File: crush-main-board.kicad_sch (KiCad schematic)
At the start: 32 parts, among them J1 4x4_Header, J10 3x3 Header, J11 3x3 Header, J12 3x2 Header, J13 3x4_Header, J14 3x4_Header, J15 2157601008, J16 Conn_01x02, J17 Conn_01x02, J2 4x4_Header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

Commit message: Fixed import issues from sch to pcb
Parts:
- J1: footprint Crush_Mainboard_Footprints:3x1_Header -> Crush_Mainboard_Footprints:4x4_Header
- U5, U6: renamed from INA232B1; value ~ -> INA232B
- U5: value ISO1640DBR -> ISO1640BDR; footprint Crush_Mainboard_Footprints:SOIC127P1030X265-16N -> Package_SO:SOIC-8_3.9x4.9mm_P1.27mm
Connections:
- net +3V3: now also U5.1 (VCC1); no longer U5.3 (VCC1)
- net +3V3_T: now also U5.8 (VCC2); no longer U5.14 (VCC2)
- net GND_T: now also U5.4 (GND1), U5.5 (GND2); no longer U5.7 (GND1), U5.9 (GND2)
- net SCL_3V3: now also U5.3 (SCL1); no longer U5.6 (SCL1)
- net SCL_T: now also U5.6 (SCL2); no longer U5.11 (SCL2)
- net SDA_3V3: now also U5.2 (SDA1); no longer U5.5 (SDA1)
- net SDA_T: now also U5.7 (SDA2); no longer U5.12 (SDA2)
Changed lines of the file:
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@@
       (effects (font (size 1.27 1.27)))
     )
-    (property "Footprint" "Crush_Mainboard_Footprints:3x1_Header" (at 255.8034 281.2796 0)
+    (property "Footprint" "Crush_Mainboard_Footprints:4x4_Header" (at 255.8034 281.2796 0)
       (effects (font (size 1.27 1.27)) (justify bottom) hide)
     )
@@
   )
   (symbol (lib_id "Crush_MainBoard_Symbols:INA232") (at 154.94 77.47 0) (unit 1)
-    (in_bom yes) (on_board yes) (dnp no) (fields_autoplaced)
-    (property "Reference" "INA232B1" (at 157.1341 66.04 0)
+    (in_bom yes) (on_board yes) (dnp no)
+    (property "Reference" "U5" (at 158.115 64.77 0)
       (effects (font (size 1.27 1.27)) (justify left))
     )
-    (property "Value" "~" (at 154.94 78.74 0)
+    (property "Value" "INA232B" (at 160.02 67.31 0)
       (effects (font (size 1.27 1.27)))
     )
@@
       (project "crush-main-board"
         (path "/74b566fe-9d71-4817-95ed-d472d647f8c8"
-          (reference "INA232B2") (unit 1)
+          (reference "U5") (unit 1)
         )
       )
@@
       (effects (font (size 1.27 1.27)))
     )
-    (property "Value" "ISO1640DBR" (at 205.74 114.3 0)
-      (effects (font (size 1.27 1.27)))
-    )
-    (property "Footprint" "Crush_Mainboard_Footprints:SOIC127P1030X265-16N" (at 205.74 134.62 0)
+    (property "Value" "ISO1640BDR" (at 205.74 114.3 0)
+      (effects (font (size 1.27 1.27)))
+    )
+    (property "Footprint" "Package_SO:SOIC-8_3.9x4.9mm_P1.27mm" (at 205.74 134.62 0)
       (effects (font (size 1.27 1.27)) hide)
     )
@@
       (effects (font (size 1.27 1.27)) hide)
     )
-    (pin "11")
-    (pin "12")
-    (pin "14")
+    (pin "1")
+    (pin "2")
+    (pin "8")
     (pin "3")
     (pin "5")
     (pin "6")
     (pin "7")
-    (pin "9")
+    (pin "4")
     (instances
       (project "battery_monitor"
@@
   )
   (symbol (lib_id "Connector_Generic:Conn_01x02") (at 234.95 210.82 180) (unit 1)
-    (in_bom yes) (on_board yes) (dnp no) (fields_autoplaced)
-    (property "Reference" "J16" (at 234.95 203.2 0)
+    (in_bom yes) (on_board yes) (dnp no)
+    (property "Reference" "J16" (at 231.14 209.55 0)
       (effects (font (size 1.27 1.27)))
     )
@@
   )
   (symbol (lib_id "Crush_MainBoard_Symbols:INA232") (at 154.94 128.27 0) (unit 1)
-    (in_bom yes) (on_board yes) (dnp no) (fields_autoplaced)
-    (property "Reference" "INA232B1" (at 157.1341 116.84 0)
+    (in_bom yes) (on_board yes) (dnp no)
+    (property "Reference" "U6" (at 157.48 115.57 0)
       (effects (font (size 1.27 1.27)) (justify left))
     )
-    (property "Value" "~" (at 154.94 129.54 0)
+    (property "Value" "INA232B" (at 160.02 118.11 0)
       (effects (font (size 1.27 1.27)))
     )
@@
       (project "crush-main-board"
         (path "/74b566fe-9d71-4817-95ed-d472d647f8c8"
-          (reference "INA232B1") (unit 1)
+          (reference "U6") (unit 1)
         )
       )
@@
   )
   (symbol (lib_id "Connector_Generic:Conn_01x02") (at 234.95 219.71 180) (unit 1)
-    (in_bom yes) (on_board yes) (dnp no) (fields_autoplaced)
-    (property "Reference" "J17" (at 234.95 212.09 0)
-      (effects (font (size 1.27 1.27)))
-    )
+    (in_bom yes) (on_board yes) (dnp no)
+    (property "Reference" "J17" (at 230.505 218.44 0)
+      (effects (font (size 1.27 1.27)))
+    )

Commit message: basic routing
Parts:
- added H1, H2, H3, H4: MountingHole_Pad, MountingHole:MountingHole_4.3mm_M4_Pad_Via, symbol Mechanical:MountingHole_Pad
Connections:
- net GND: now also H1.1, H2.1, H3.1, H4.1
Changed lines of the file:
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@@
     (rev "1")
   )
+  (junction (at 377.19 149.86) (diameter 0) (color 0 0 0 0)
+  )
+  (junction (at 377.19 154.94) (diameter 0) (color 0 0 0 0)
+  )
   (junction (at 97.155 252.73) (diameter 0) (color 0 0 0 0)
   )
@@
   (junction (at 321.31 253.365) (diameter 0) (color 0 0 0 0)
   )
+  (junction (at 377.19 144.78) (diameter 0) (color 0 0 0 0)
+  )
   (junction (at 321.31 206.375) (diameter 0) (color 0 0 0 0)
   )
@@
     (stroke (width 0) (type default))
   )
+  (wire (pts (xy 377.19 157.48) (xy 377.19 154.94))
+    (stroke (width 0) (type default))
+  )
   (wire (pts (xy 290.83 213.36) (xy 290.83 215.9))
     (stroke (width 0) (type default))
@@
     (stroke (width 0) (type default))
   )
+  (wire (pts (xy 377.19 154.94) (xy 379.73 154.94))
+    (stroke (width 0) (type default))
+  )
   (wire (pts (xy 239.2934 270.4846) (xy 241.8334 270.4846))
     (stroke (width 0) (type default))
@@
     (stroke (width 0) (type default))
   )
+  (wire (pts (xy 377.19 144.78) (xy 379.73 144.78))
+    (stroke (width 0) (type default))
+  )
   (wire (pts (xy 386.08 42.545) (xy 386.08 45.085))
     (stroke (width 0) (type default))
@@
     (stroke (width 0) (type default))
   )
+  (wire (pts (xy 377.19 149.86) (xy 377.19 144.78))
+    (stroke (width 0) (type default))
+  )
   (wire (pts (xy 239.2934 267.9446) (xy 239.2934 270.4846))
     (stroke (width 0) (type default))
@@
     (stroke (width 0) (type default))
   )
+  (wire (pts (xy 377.19 144.78) (xy 377.19 139.7))
+    (stroke (width 0) (type default))
+  )
   (wire (pts (xy 321.31 253.365) (xy 321.31 250.825))
     (stroke (width 0) (type default))
@@
     (stroke (width 0) (type default))
   )
+  (wire (pts (xy 377.19 149.86) (xy 379.73 149.86))
+    (stroke (width 0) (type default))
+  )
   (wire (pts (xy 97.155 255.27) (xy 94.615 255.27))
     (stroke (width 0) (type default))
@@
     (stroke (width 0) (type default))
   )
+  (wire (pts (xy 377.19 139.7) (xy 379.73 139.7))
+    (stroke (width 0) (type default))
+  )
   (wire (pts (xy 194.31 106.68) (xy 193.04 106.68))
     (stroke (width 0) (type default))
@@
     (stroke (width 0) (type default))
   )
+  (wire (pts (xy 377.19 154.94) (xy 377.19 149.86))
+    (stroke (width 0) (type default))
+  )
   (wire (pts (xy 162.56 255.27) (xy 162.56 257.81))
     (stroke (width 0) (type default))
@@
     (effects (font (size 2 2)) (justify left top))
   )
+  (text_box "Mounting Holes"
+    (at 373.38 133.35 0) (size 33.02 31.75)
+    (stroke (width 0) (type dash))
+    (fill (type none))
+    (effects (font (size 1.27 1.27)) (justify left top))
+  )
   (text_box "Analog&Digital_Headers"
     (at 12.827 209.169 0) (size 91.694 73.66)
@@
     )
   )
+  (symbol (lib_id "Mechanical:MountingHole_Pad") (at 382.27 139.7 270) (unit 1)
+    (in_bom yes) (on_board yes) (dnp no) (fields_autoplaced)
+    (property "Reference" "H1" (at 386.08 138.43 90)
+      (effects (font (size 1.27 1.27)) (justify left))
+    )
+    (property "Value" "MountingHole_Pad" (at 386.08 140.97 90)
+      (effects (font (size 1.27 1.27)) (justify left))
+    )
+    (property "Footprint" "MountingHole:MountingHole_4.3mm_M4_Pad_Via" (at 382.27 139.7 0)
+      (effects (font (size 1.27 1.27)) hide)
+    )
+    (property "Datasheet" "" (at 382.27 139.7 0)
+      (effects (font (size 1.27 1.27)) hide)
+    )
+    (pin "1")
+    (instances
+      (project "crush-main-board"
+        (path "/74b566fe-9d71-4817-95ed-d472d647f8c8"
+          (reference "H1") (unit 1)
+        )
+      )
+    )
+  )
   (symbol (lib_id "power:GND") (at 66.675 274.955 0) (mirror y) (unit 1)
     (in_bom yes) (on_board yes) (dnp no)
@@
     )
   )
+  (symbol (lib_id "Mechanical:MountingHole_Pad") (at 382.27 154.94 270) (unit 1)
+    (in_bom yes) (on_board yes) (dnp no) (fields_autoplaced)
+    (property "Reference" "H4" (at 386.08 153.67 90)
+      (effects (font (size 1.27 1.27)) (justify left))
+    )
+    (property "Value" "MountingHole_Pad" (at 386.08 156.21 90)
+      (effects (font (size 1.27 1.27)) (justify left))
+    )
+    (property "Footprint" "MountingHole:MountingHole_4.3mm_M4_Pad_Via" (at 382.27 154.94 0)
+      (effects (font (size 1.27 1.27)) hide)
+    )
+    (property "Datasheet" "~" (at 382.27 154.94 0)
+      (effects (font (size 1.27 1.27)) hide)
+    )
+    (pin "1")
+    (instances
+      (project "crush-main-board"
+        (path "/74b566fe-9d71-4817-95ed-d472d647f8c8"
+          (reference "H4") (unit 1)
+        )
+      )
+    )
+  )
   (symbol (lib_id "power:+3V3") (at 151.13 54.61 0) (unit 1)
     (in_bom yes) (on_board yes) (dnp no) (fields_autoplaced)
@@
     )
   )
+  (symbol (lib_id "Mechanical:MountingHole_Pad") (at 382.27 144.78 270) (unit 1)
+    (in_bom yes) (on_board yes) (dnp no) (fields_autoplaced)
+    (property "Reference" "H2" (at 386.08 143.51 90)
+      (effects (font (size 1.27 1.27)) (justify left))
+    )
+    (property "Value" "MountingHole_Pad" (at 386.08 146.05 90)
+      (effects (font (size 1.27 1.27)) (justify left))
+    )
+    (property "Footprint" "MountingHole:MountingHole_4.3mm_M4_Pad_Via" (at 382.27 144.78 0)
+      (effects (font (size 1.27 1.27)) hide)
+    )
+    (property "Datasheet" "~" (at 382.27 144.78 0)
+      (effects (font (size 1.27 1.27)) hide)
+    )
+    (pin "1")
+    (instances
+      (project "crush-main-board"
+        (path "/74b566fe-9d71-4817-95ed-d472d647f8c8"
+          (reference "H2") (unit 1)
+        )
+      )
+    )
+  )
   (symbol (lib_id "Connector_Generic:Conn_01x02") (at 234.95 210.82 180) (unit 1)
     (in_bom yes) (on_board yes) (dnp no)
@@
     )
   )
+  (symbol (lib_id "power:GND") (at 377.19 157.48 0) (mirror y) (unit 1)
+    (in_bom yes) (on_board yes) (dnp no)
+    (property "Reference" "#PWR061" (at 377.19 163.83 0)
+      (effects (font (size 1.27 1.27)) hide)
+    )
+    (property "Value" "GND" (at 377.19 162.56 0)
+      (effects (font (size 1.27 1.27)))
+    )
+    (property "Footprint" "" (at 377.19 157.48 0)
+      (effects (font (size 1.27 1.27)) hide)
+    )
+    (property "Datasheet" "" (at 377.19 157.48 0)
+      (effects (font (size 1.27 1.27)) hide)
+    )
+    (pin "1")
+    (instances
+      (project "crush-main-board"
+        (path "/74b566fe-9d71-4817-95ed-d472d647f8c8"
+          (reference "#PWR061") (unit 1)
+        )
+      )
+    )
+  )
   (symbol (lib_id "Crush_MainBoard_Symbols:+3V3_T") (at 181.61 106.68 0) (unit 1)
     (in_bom yes) (on_board yes) (dnp no)
@@
         )
       )
+    )
+  )
+  (symbol (lib_id "Mechanical:MountingHole_Pad") (at 382.27 149.86 270) (unit 1)
+    (in_bom yes) (on_board yes) (dnp no) (fields_autoplaced)
+    (property "Reference" "H3" (at 386.08 148.59 90)
+      (effects (font (size 1.27 1.27)) (justify left))
+    )
+    (property "Value" "MountingHole_Pad" (at 386.08 151.13 90)
+      (effects (font (size 1.27 1.27)) (justify left))
+    )
+    (property "Footprint" "MountingHole:MountingHole_4.3mm_M4_Pad_Via" (at 382.27 149.86 0)
+      (effects (font (size 1.27 1.27)) hide)
+    )
+    (property "Datasheet" "~" (at 382.27 149.86 0)
+      (effects (font (size 1.27 1.27)) hide)
+    )
+    (pin "1")
+    (instances
+      (project "crush-main-board"
+        (path "/74b566fe-9d71-4817-95ed-d472d647f8c8"
+          (reference "H3") (unit 1)
+        )
+      )

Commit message: place mounting holes
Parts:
- H1, H2, H3, H4: footprint MountingHole:MountingHole_4.3mm_M4_Pad_Via -> MountingHole:MountingHole_3.7mm_Pad_Via
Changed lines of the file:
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@@
       (effects (font (size 1.27 1.27)) (justify left))
     )
-    (property "Footprint" "MountingHole:MountingHole_4.3mm_M4_Pad_Via" (at 382.27 139.7 0)
+    (property "Footprint" "MountingHole:MountingHole_3.7mm_Pad_Via" (at 382.27 139.7 0)
       (effects (font (size 1.27 1.27)) hide)
     )
@@
       (effects (font (size 1.27 1.27)) (justify left))
     )
-    (property "Footprint" "MountingHole:MountingHole_4.3mm_M4_Pad_Via" (at 382.27 154.94 0)
+    (property "Footprint" "MountingHole:MountingHole_3.7mm_Pad_Via" (at 382.27 154.94 0)
       (effects (font (size 1.27 1.27)) hide)
     )
@@
       (effects (font (size 1.27 1.27)) (justify left))
     )
-    (property "Footprint" "MountingHole:MountingHole_4.3mm_M4_Pad_Via" (at 382.27 144.78 0)
+    (property "Footprint" "MountingHole:MountingHole_3.7mm_Pad_Via" (at 382.27 144.78 0)
       (effects (font (size 1.27 1.27)) hide)
     )
@@
       (effects (font (size 1.27 1.27)) (justify left))
     )
-    (property "Footprint" "MountingHole:MountingHole_4.3mm_M4_Pad_Via" (at 382.27 149.86 0)
-      (effects (font (size 1.27 1.27)) hide)
-    )
+    (property "Footprint" "MountingHole:MountingHole_3.7mm_Pad_Via" (at 382.27 149.86 0)
+      (effects (font (size 1.27 1.27)) hide)
+    )

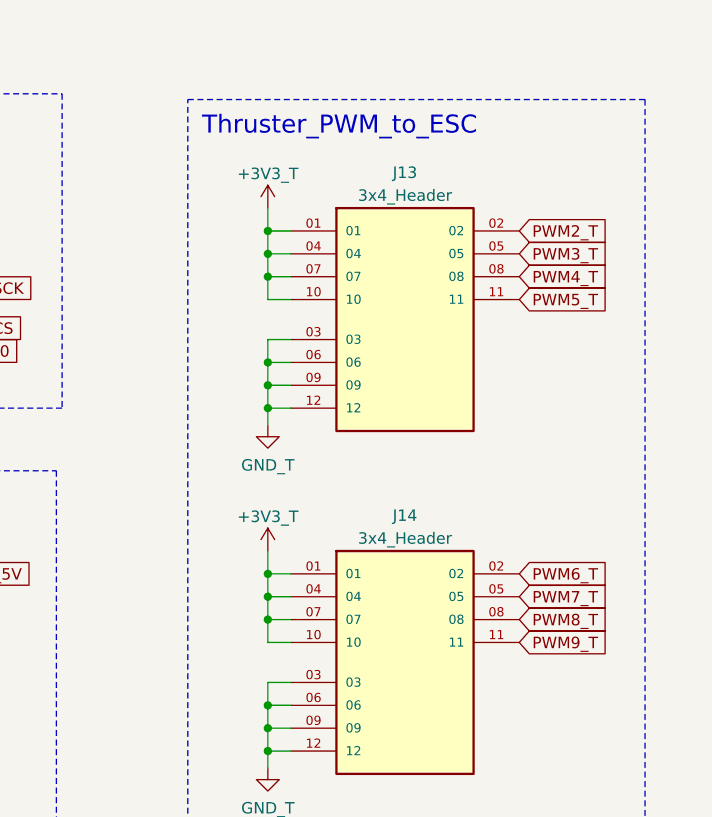
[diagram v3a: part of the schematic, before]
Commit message: fix thruster headers
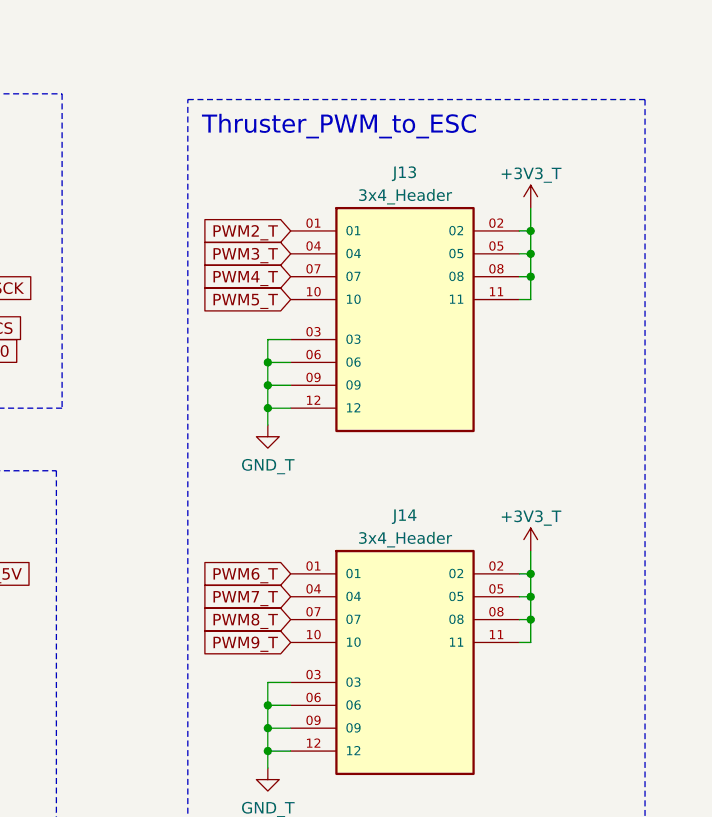
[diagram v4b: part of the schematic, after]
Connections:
- net +3V3_T: now also J13.02, J13.05, J13.08, J13.11, J14.02, J14.05, J14.08, J14.11; no longer J13.01, J13.04, J13.07, J13.10, J14.01, J14.04, J14.07, J14.10
- net PWM2_T: now also J13.01; no longer J13.02
- net PWM3_T: now also J13.04; no longer J13.05
- net PWM4_T: now also J13.07; no longer J13.08
- net PWM5_T: now also J13.10; no longer J13.11
- net PWM6_T: now also J14.01; no longer J14.02
- net PWM7_T: now also J14.04; no longer J14.05
- net PWM8_T: now also J14.07; no longer J14.08
- net PWM9_T: now also J14.10; no longer J14.11

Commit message: schematic net fixes
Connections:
- net +3V3: no longer C2.2, U2.16 (VCC2)
- net +3V3_T: now also C2.2, U2.16 (VCC2)
- net BATT: no longer J15.6, U6.1 (Vin+), U6.2 (Vin-)
- net GND: now also U5.5 (GND2)
- net GND_T: no longer U5.5 (GND2)
- new net BATT_T: J15.6, U6.1 (Vin+), U6.2 (Vin-)
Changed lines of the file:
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@@
     (effects (font (size 1.27 1.27)) (justify left bottom))
   )
-  (label "16V8 (MAX)" (at 129.54 125.73 0) (fields_autoplaced)
+  (label "16V8_T (MAX)" (at 129.54 125.73 0) (fields_autoplaced)
     (effects (font (size 1.27 1.27)) (justify left bottom))
   )
@@
   (global_label "BATT_T" (shape input) (at 20.32 186.69 180) (fields_autoplaced)
     (effects (font (size 1.27 1.27)) (justify right))
-    (property "Intersheetrefs" "${INTERSHEET_REFS}" (at 11.1852 186.69 0)
+    (property "Intersheetrefs" "${INTERSHEET_REFS}" (at 11.1058 186.69 0)
       (effects (font (size 1.27 1.27)) (justify right) hide)
     )
@@
     (property "Intersheetrefs" "${INTERSHEET_REFS}" (at 393.7633 28.575 0)
       (effects (font (size 1.27 1.27)) (justify left) hide)
+    )
+  )
+  (symbol (lib_id "power:GND") (at 193.04 134.62 0) (unit 1)
+    (in_bom yes) (on_board yes) (dnp no)
+    (property "Reference" "#PWR067" (at 193.04 140.97 0)
+      (effects (font (size 1.27 1.27)) hide)
+    )
+    (property "Value" "GND" (at 193.04 139.065 0)
+      (effects (font (size 1.27 1.27)))
+    )
+    (property "Footprint" "" (at 193.04 134.62 0)
+      (effects (font (size 1.27 1.27)) hide)
+    )
+    (property "Datasheet" "" (at 193.04 134.62 0)
+      (effects (font (size 1.27 1.27)) hide)
+    )
+    (pin "1")
+    (instances
+      (project "crush-main-board"
+        (path "/74b566fe-9d71-4817-95ed-d472d647f8c8"
+          (reference "#PWR067") (unit 1)
+        )
+      )
     )
   )
@@
     )
   )
-  (symbol (lib_id "Crush_MainBoard_Symbols:GND_T") (at 193.04 134.62 0) (mirror y) (unit 1)
-    (in_bom yes) (on_board yes) (dnp no)
-    (property "Reference" "#PWR067" (at 193.04 140.97 0)
-      (effects (font (size 1.27 1.27)) hide)
-    )
-    (property "Value" "GND_T" (at 193.04 139.065 0)
-      (effects (font (size 1.27 1.27)))
-    )
-    (property "Footprint" "" (at 193.04 134.62 0)
-      (effects (font (size 1.27 1.27)) hide)
-    )
-    (property "Datasheet" "" (at 193.04 134.62 0)
-      (effects (font (size 1.27 1.27)) hide)
-    )
-    (pin "1")
-    (instances
-      (project "crush-main-board"
-        (path "/74b566fe-9d71-4817-95ed-d472d647f8c8"
-          (reference "#PWR067") (unit 1)
-        )
-      )
-    )
-  )
   (symbol (lib_id "Crush_MainBoard_Symbols:GND_T") (at 36.83 193.04 0) (unit 1)
     (in_bom yes) (on_board yes) (dnp no)
@@
     )
   )
-  (symbol (lib_id "power:+3V3") (at 386.08 15.875 0) (mirror y) (unit 1)
+  (symbol (lib_id "Crush_MainBoard_Symbols:+3V3_T") (at 386.08 15.875 0) (mirror y) (unit 1)
     (in_bom yes) (on_board yes) (dnp no) (fields_autoplaced)
     (property "Reference" "#PWR010" (at 386.08 19.685 0)
       (effects (font (size 1.27 1.27)) hide)
     )
-    (property "Value" "+3V3_T" (at 386.08 12.065 0)
-      (effects (font (size 1.27 1.27)))
-    )
+    (property "Value" "+3V3_T" (at 386.08 11.43 0)
+      (effects (font (size 1.27 1.27)))
+    )

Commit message: more schematic fixes
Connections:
- net GND: now also U5.4 (GND1); no longer U5.5 (GND2)
- net GND_T: now also U5.5 (GND2); no longer U5.4 (GND1)
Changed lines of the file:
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@@
-    )
-  )
-  (symbol (lib_id "power:GND") (at 193.04 134.62 0) (unit 1)
-    (in_bom yes) (on_board yes) (dnp no)
-    (property "Reference" "#PWR067" (at 193.04 140.97 0)
-      (effects (font (size 1.27 1.27)) hide)
-    )
-    (property "Value" "GND" (at 193.04 139.065 0)
-      (effects (font (size 1.27 1.27)))
-    )
-    (property "Footprint" "" (at 193.04 134.62 0)
-      (effects (font (size 1.27 1.27)) hide)
-    )
-    (property "Datasheet" "" (at 193.04 134.62 0)
-      (effects (font (size 1.27 1.27)) hide)
-    )
-    (pin "1")
-    (instances
-      (project "crush-main-board"
-        (path "/74b566fe-9d71-4817-95ed-d472d647f8c8"
-          (reference "#PWR067") (unit 1)
-        )
-      )
     )
   )
@@
         (path "/74b566fe-9d71-4817-95ed-d472d647f8c8"
           (reference "#PWR068") (unit 1)
+        )
+      )
+    )
+  )
+  (symbol (lib_id "power:GND") (at 218.44 134.62 0) (unit 1)
+    (in_bom yes) (on_board yes) (dnp no)
+    (property "Reference" "#PWR069" (at 218.44 140.97 0)
+      (effects (font (size 1.27 1.27)) hide)
+    )
+    (property "Value" "GND" (at 218.44 139.065 0)
+      (effects (font (size 1.27 1.27)))
+    )
+    (property "Footprint" "" (at 218.44 134.62 0)
+      (effects (font (size 1.27 1.27)) hide)
+    )
+    (property "Datasheet" "" (at 218.44 134.62 0)
+      (effects (font (size 1.27 1.27)) hide)
+    )
+    (pin "1")
+    (instances
+      (project "crush-main-board"
+        (path "/74b566fe-9d71-4817-95ed-d472d647f8c8"
+          (reference "#PWR069") (unit 1)
         )
       )
@@
     )
   )
+  (symbol (lib_id "Crush_MainBoard_Symbols:GND_T") (at 193.04 134.62 0) (mirror y) (unit 1)
+    (in_bom yes) (on_board yes) (dnp no)
+    (property "Reference" "#PWR067" (at 193.04 140.97 0)
+      (effects (font (size 1.27 1.27)) hide)
+    )
+    (property "Value" "GND_T" (at 193.04 139.065 0)
+      (effects (font (size 1.27 1.27)))
+    )
+    (property "Footprint" "" (at 193.04 134.62 0)
+      (effects (font (size 1.27 1.27)) hide)
+    )
+    (property "Datasheet" "" (at 193.04 134.62 0)
+      (effects (font (size 1.27 1.27)) hide)
+    )
+    (pin "1")
+    (instances
+      (project "crush-main-board"
+        (path "/74b566fe-9d71-4817-95ed-d472d647f8c8"
+          (reference "#PWR067") (unit 1)
+        )
+      )
+    )
+  )
   (symbol (lib_id "Crush_MainBoard_Symbols:GND_T") (at 36.83 193.04 0) (unit 1)
     (in_bom yes) (on_board yes) (dnp no)
@@
         )
       )
-    )
-  )
-  (symbol (lib_id "Crush_MainBoard_Symbols:GND_T") (at 218.44 134.62 0) (mirror y) (unit 1)
-    (in_bom yes) (on_board yes) (dnp no)
-    (property "Reference" "#PWR069" (at 218.44 140.97 0)
-      (effects (font (size 1.27 1.27)) hide)
-    )
-    (property "Value" "GND_T" (at 218.44 139.065 0)
-      (effects (font (size 1.27 1.27)))
-    )
-    (property "Footprint" "" (at 218.44 134.62 0)
-      (effects (font (size 1.27 1.27)) hide)
-    )
-    (property "Datasheet" "" (at 218.44 134.62 0)
-      (effects (font (size 1.27 1.27)) hide)
-    )
-    (pin "1")
-    (instances
-      (project "crush-main-board"
-        (path "/74b566fe-9d71-4817-95ed-d472d647f8c8"
-          (reference "#PWR069") (unit 1)
-        )
-      )
